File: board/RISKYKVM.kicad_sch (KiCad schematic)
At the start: 19 parts, among them J2 Conn_01x02, J3 DE9_Plug, J4 Conn_01x08, J4 USB_1, U1 CH32V203C8T6, U2 LM1117MP-3.3

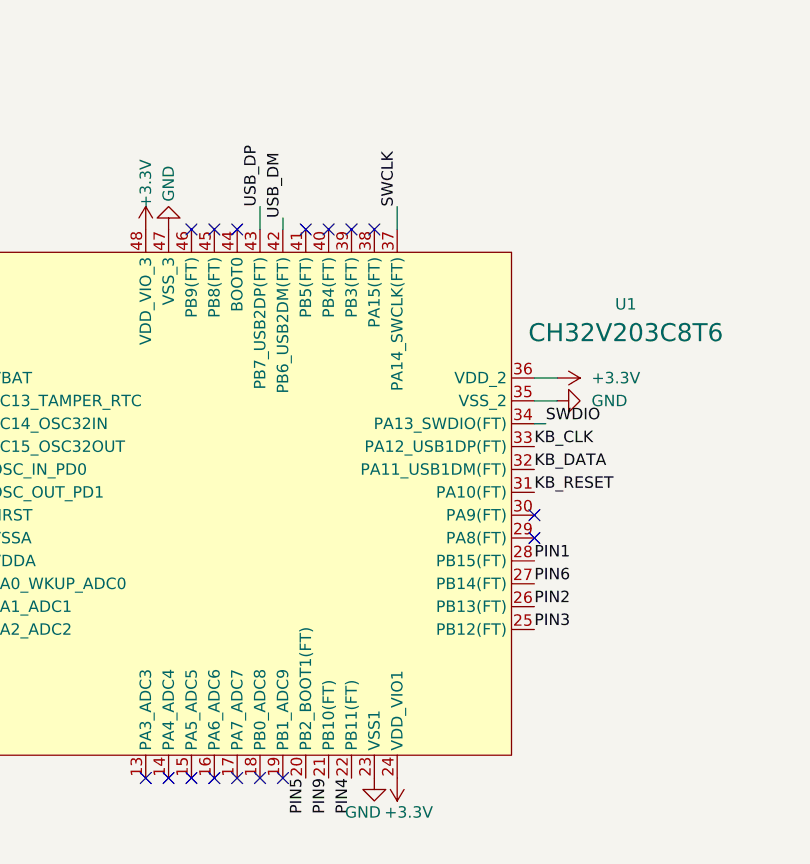
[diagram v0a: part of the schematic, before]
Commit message: Fix issues related to BOOT0 and BOOT1
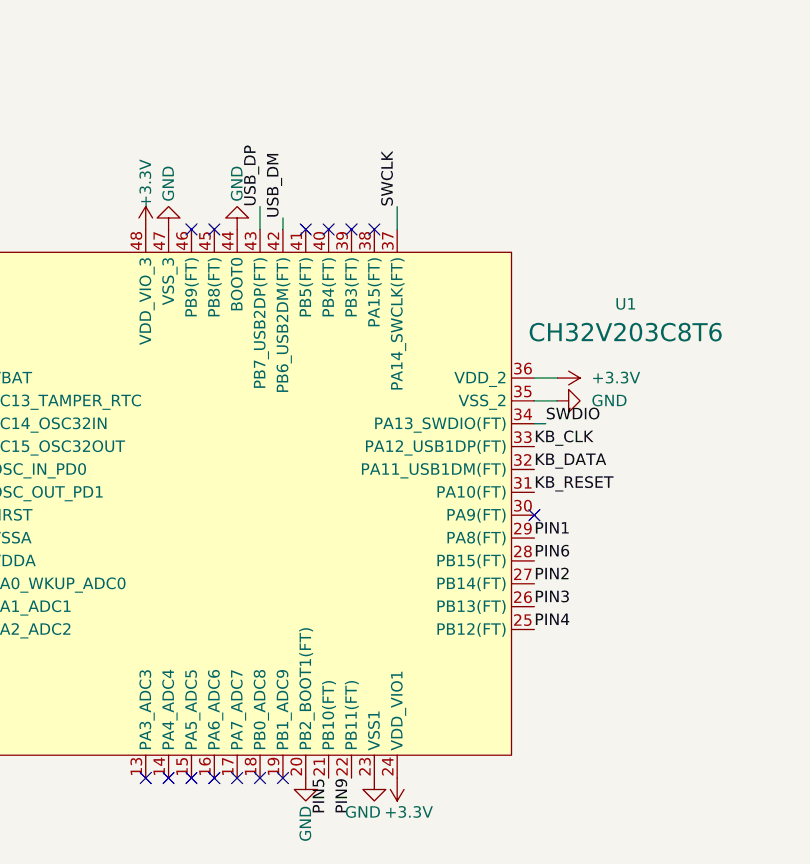
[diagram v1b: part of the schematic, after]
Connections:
- net GND: now also U1.20 (PB2_BOOT1(FT)), U1.44 (BOOT0)
- net PIN1: now also U1.29 (PA8(FT)); no longer U1.28 (PB15(FT))
- net PIN2: now also U1.27 (PB14(FT)); no longer U1.26 (PB13(FT))
- net PIN3: now also U1.26 (PB13(FT)); no longer U1.25 (PB12(FT))
- net PIN4: now also U1.25 (PB12(FT)); no longer U1.22 (PB11(FT))
- net PIN5: now also U1.21 (PB10(FT)); no longer U1.20 (PB2_BOOT1(FT))
- net PIN6: now also U1.28 (PB15(FT)); no longer U1.27 (PB14(FT))
- net PIN9: now also U1.22 (PB11(FT)); no longer U1.21 (PB10(FT))
- no-connect marks 26 -> 24
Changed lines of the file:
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@@
   (no_connect (at 69.85 101.6))
   (no_connect (at 107.95 133.35))
-  (no_connect (at 74.93 101.6))
   (no_connect (at 87.63 101.6))
   (no_connect (at 44.45 143.51))
@@
   (no_connect (at 69.85 162.56))
   (no_connect (at 74.93 162.56))
-  (no_connect (at 107.95 135.89))
   (no_connect (at 205.74 41.91))
   (no_connect (at 90.17 101.6))
@@
     (effects (font (size 1.27 1.27)) (justify left bottom))
   )
+  (label "PIN1" (at 107.95 135.89 0) (fields_autoplaced)
+    (effects (font (size 1.27 1.27)) (justify left bottom))
+  )
   (label "PIN2" (at 229.87 135.89 180) (fields_autoplaced)
     (effects (font (size 1.27 1.27)) (justify right bottom))
   )
-  (label "PIN5" (at 82.55 162.56 270) (fields_autoplaced)
-    (effects (font (size 1.27 1.27)) (justify right bottom))
-  )
   (label "USB_DM" (at 80.01 100.33 90) (fields_autoplaced)
     (effects (font (size 1.27 1.27)) (justify left bottom))
@@
     (effects (font (size 1.27 1.27)) (justify right bottom))
   )
-  (label "PIN9" (at 85.09 162.56 270) (fields_autoplaced)
-    (effects (font (size 1.27 1.27)) (justify right bottom))
-  )
   (label "LED1" (at 170.18 92.71 180) (fields_autoplaced)
     (effects (font (size 1.27 1.27)) (justify right bottom))
@@
     (effects (font (size 1.27 1.27)) (justify left bottom))
   )
+  (label "PIN5" (at 85.09 162.56 270) (fields_autoplaced)
+    (effects (font (size 1.27 1.27)) (justify right bottom))
+  )
   (label "PIN3" (at 229.87 130.81 180) (fields_autoplaced)
     (effects (font (size 1.27 1.27)) (justify right bottom))
   )
-  (label "PIN3" (at 107.95 146.05 0) (fields_autoplaced)
-    (effects (font (size 1.27 1.27)) (justify left bottom))
-  )
-  (label "PIN6" (at 107.95 140.97 0) (fields_autoplaced)
-    (effects (font (size 1.27 1.27)) (justify left bottom))
-  )
-  (label "PIN4" (at 87.63 162.56 270) (fields_autoplaced)
-    (effects (font (size 1.27 1.27)) (justify right bottom))
-  )
   (label "PIN1" (at 229.87 140.97 180) (fields_autoplaced)
     (effects (font (size 1.27 1.27)) (justify right bottom))
@@
     (effects (font (size 1.27 1.27)) (justify right bottom))
   )
+  (label "PIN3" (at 107.95 143.51 0) (fields_autoplaced)
+    (effects (font (size 1.27 1.27)) (justify left bottom))
+  )
   (label "SWDIO" (at 109.22 123.19 0) (fields_autoplaced)
     (effects (font (size 1.27 1.27)) (justify left bottom))
@@
     (effects (font (size 1.27 1.27)) (justify right bottom))
   )
+  (label "PIN6" (at 107.95 138.43 0) (fields_autoplaced)
+    (effects (font (size 1.27 1.27)) (justify left bottom))
+  )
   (label "USB_DP" (at 161.29 38.1 180) (fields_autoplaced)
     (effects (font (size 1.27 1.27)) (justify right bottom))
   )
-  (label "PIN2" (at 107.95 143.51 0) (fields_autoplaced)
+  (label "PIN4" (at 107.95 146.05 0) (fields_autoplaced)
     (effects (font (size 1.27 1.27)) (justify left bottom))
   )
@@
     (effects (font (size 1.27 1.27)) (justify left bottom))
   )
-  (label "PIN1" (at 107.95 138.43 0) (fields_autoplaced)
+  (label "PIN9" (at 87.63 162.56 270) (fields_autoplaced)
+    (effects (font (size 1.27 1.27)) (justify right bottom))
+  )
+  (label "PIN2" (at 107.95 140.97 0) (fields_autoplaced)
     (effects (font (size 1.27 1.27)) (justify left bottom))
   )
@@
         (path "/f833f147-620f-4e1d-8728-dea16845f2b9"
           (reference "J3") (unit 1)
+        )
+      )
+    )
+  )
+  (symbol (lib_id "power:GND") (at 74.93 101.6 180) (unit 1)
+    (in_bom yes) (on_board yes) (dnp no)
+    (property "Reference" "#PWR010" (at 74.93 95.25 0)
+      (effects (font (size 1.27 1.27)) hide)
+    )
+    (property "Value" "GND" (at 74.93 96.52 90)
+      (effects (font (size 1.27 1.27)))
+    )
+    (property "Footprint" "" (at 74.93 101.6 0)
+      (effects (font (size 1.27 1.27)) hide)
+    )
+    (property "Datasheet" "" (at 74.93 101.6 0)
+      (effects (font (size 1.27 1.27)) hide)
+    )
+    (pin "1")
+    (instances
+      (project "MSXMouseCH32V103C"
+        (path "/39121b1a-257d-4846-897b-f35d40c1dadd"
+          (reference "#PWR010") (unit 1)
+        )
+      )
+      (project "RISKYKVM"
+        (path "/f833f147-620f-4e1d-8728-dea16845f2b9"
+          (reference "#PWR015") (unit 1)
         )
       )
@@
         )
       )
+    )
+  )
+  (symbol (lib_id "power:GND") (at 82.55 162.56 0) (unit 1)
+    (in_bom yes) (on_board yes) (dnp no)
+    (property "Reference" "#PWR010" (at 82.55 168.91 0)
+      (effects (font (size 1.27 1.27)) hide)
+    )
+    (property "Value" "GND" (at 82.55 167.64 90)
+      (effects (font (size 1.27 1.27)))
+    )
+    (property "Footprint" "" (at 82.55 162.56 0)
+      (effects (font (size 1.27 1.27)) hide)
+    )
+    (property "Datasheet" "" (at 82.55 162.56 0)
+      (effects (font (size 1.27 1.27)) hide)
+    )
+    (pin "1")
+    (instances
+      (project "MSXMouseCH32V103C"
+        (path "/39121b1a-257d-4846-897b-f35d40c1dadd"
+          (reference "#PWR010") (unit 1)
+        )
+      )
+      (project "RISKYKVM"
+        (path "/f833f147-620f-4e1d-8728-dea16845f2b9"
+          (reference "#PWR016") (unit 1)
+        )
+      )

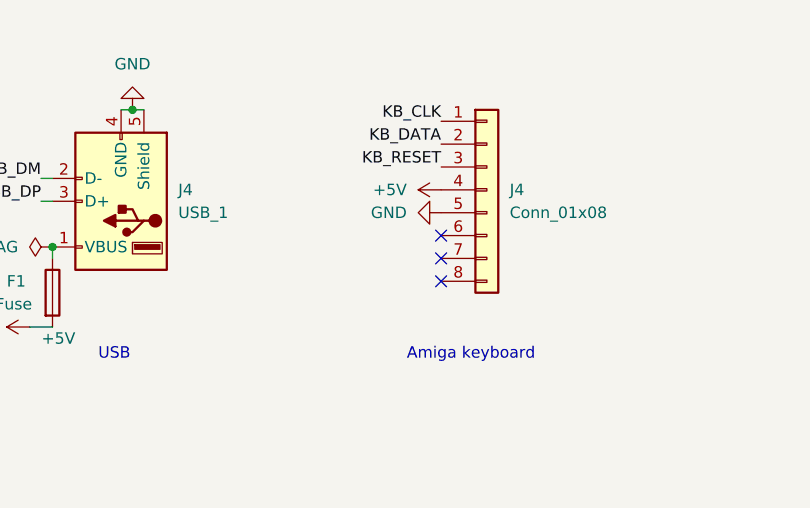
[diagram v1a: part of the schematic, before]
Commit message: KEY in Amiga Port missing
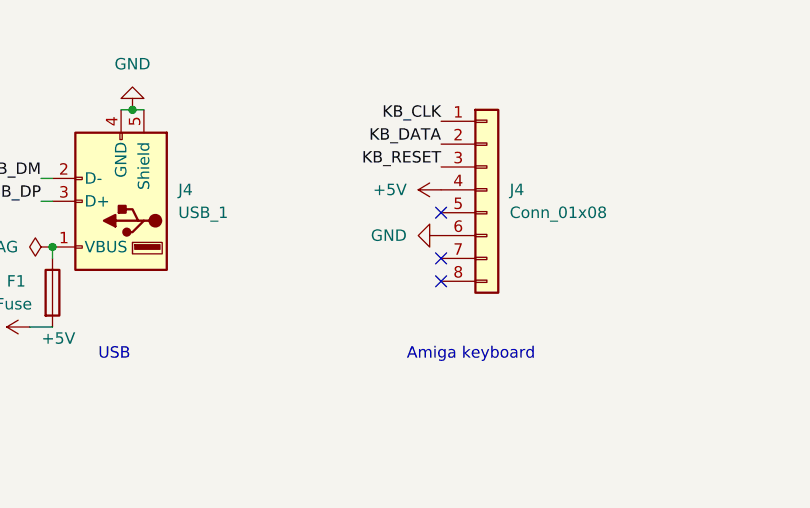
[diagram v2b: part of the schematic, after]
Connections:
- net GND: now also J4.6 (Pin_6); no longer J4.5 (Pin_5)
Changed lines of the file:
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@@
   (no_connect (at 44.45 128.27))
   (no_connect (at 85.09 101.6))
+  (no_connect (at 205.74 39.37))
   (no_connect (at 69.85 162.56))
   (no_connect (at 74.93 162.56))
-  (no_connect (at 205.74 41.91))
   (no_connect (at 90.17 101.6))
   (no_connect (at 72.39 162.56))
@@
         (path "/f833f147-620f-4e1d-8728-dea16845f2b9"
           (reference "C2") (unit 1)
+        )
+      )
+    )
+  )
+  (symbol (lib_id "power:GND") (at 205.74 41.91 270) (unit 1)
+    (in_bom yes) (on_board yes) (dnp no) (fields_autoplaced)
+    (property "Reference" "#PWR020" (at 199.39 41.91 0)
+      (effects (font (size 1.27 1.27)) hide)
+    )
+    (property "Value" "GND" (at 201.93 41.91 90)
+      (effects (font (size 1.27 1.27)) (justify right))
+    )
+    (property "Footprint" "" (at 205.74 41.91 0)
+      (effects (font (size 1.27 1.27)) hide)
+    )
+    (property "Datasheet" "" (at 205.74 41.91 0)
+      (effects (font (size 1.27 1.27)) hide)
+    )
+    (pin "1")
+    (instances
+      (project "RISKYKVM"
+        (path "/f833f147-620f-4e1d-8728-dea16845f2b9"
+          (reference "#PWR020") (unit 1)
         )
       )
@@
         )
       )
-    )
-  )
-  (symbol (lib_id "power:GND") (at 205.74 39.37 270) (unit 1)
-    (in_bom yes) (on_board yes) (dnp no) (fields_autoplaced)
-    (property "Reference" "#PWR020" (at 199.39 39.37 0)
-      (effects (font (size 1.27 1.27)) hide)
-    )
-    (property "Value" "GND" (at 201.93 39.37 90)
-      (effects (font (size 1.27 1.27)) (justify right))
-    )
-    (property "Footprint" "" (at 205.74 39.37 0)
-      (effects (font (size 1.27 1.27)) hide)
-    )
-    (property "Datasheet" "" (at 205.74 39.37 0)
-      (effects (font (size 1.27 1.27)) hide)
-    )
-    (pin "1")
-    (instances
-      (project "RISKYKVM"
-        (path "/f833f147-620f-4e1d-8728-dea16845f2b9"
-          (reference "#PWR020") (unit 1)
-        )
-      )
